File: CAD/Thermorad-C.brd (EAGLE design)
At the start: 177.5 x 33.6 mm, 84 parts, among them IC1 LM324D, IC2 TPS61070DDC, IC4 LM324D, J1 DNP, SW1 450404015514, SW2 450404015514, T1 DNP, U1 ADL5910, U2 LM2936M-3.3, U3 LM2936M-5.0/DNP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

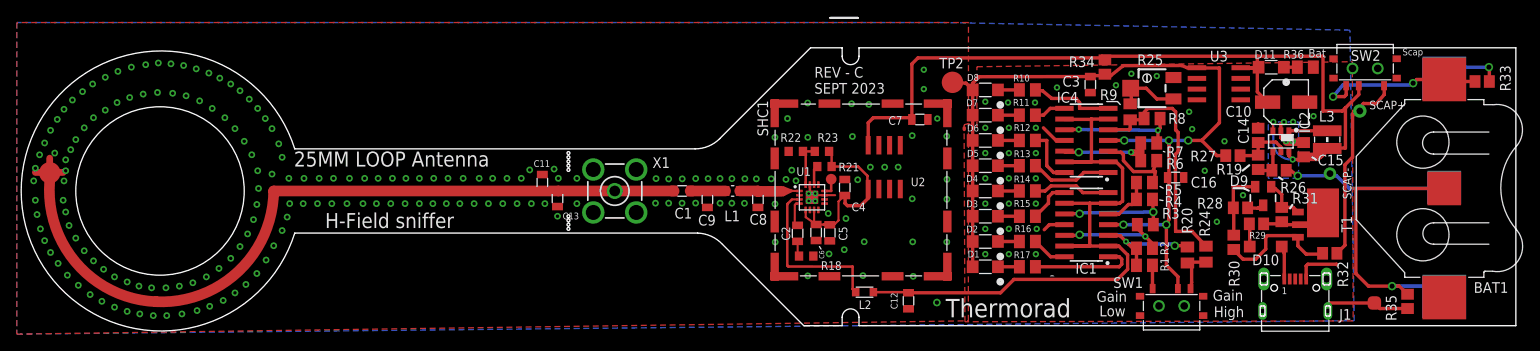
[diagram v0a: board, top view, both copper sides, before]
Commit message: Update C - Cheaper Potentiometer implanted
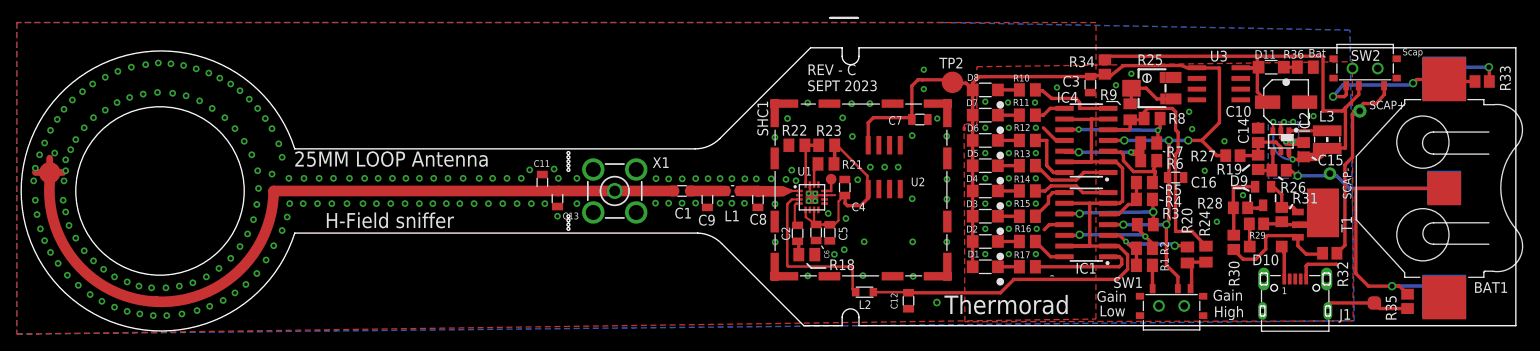
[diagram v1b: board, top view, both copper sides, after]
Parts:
- C1: value CBF/0805/742792037 -> CSGP/0805/1µF/885012107015
- C11, C13: value 1N4148 -> DNP/1N4148
- C9: value !RES/0805/82R -> DNP/!RES/0805/82R
- L1: value CAP/0805/470pF/NP0 -> RES/0805/82R/5%
- L2: value RES/0805/1k -> RES/0805/10k
- R10, R11: value 10k -> 2k2
- R15: value 1K -> 10k
- R16, R17: value 1k -> 10k
- R18: device rcl:R0603 -> resistor:M0805
- R21, R22, R23: value 0603/10k -> 10k; device rcl:R0603 -> resistor:M0805
- SHC1: value 36103205S -> DNP/36103205S
- X1: value BU-SMA-V -> DNP/BU-SMA-V
- moved R23 0.93 mm to (106.2, 20.4)
- moved R22 0.74 mm to (102.6, 20.4)
- moved R21 0.36 mm to (106.1, 18.2), turned to 180 degrees
- moved R18 0.18 mm to (103.8, 7.44)
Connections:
- net +3V3: now also R21.1; no longer R21.2
- net N$36: now also R21.2; no longer R21.1
- net VDD: now also C7.2, U2.8
- net VEE: no longer C7.2, U2.8
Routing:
- net VEE: track 107.4 -> 69.5 mm
- net VDD: track 108.9 -> 126.3 mm
- net N$38: track 5.48 -> 6.36 mm
- net +3V3: track 26.0 -> 26.8 mm
- net N$36: track 2.31 -> 2.83 mm
- net GND: vias 235 -> 234
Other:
- board text removed: "C:/Users/sylvain.lebras/Documents/eagle/Logo.bmp"
